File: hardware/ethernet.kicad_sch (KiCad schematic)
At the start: 98 parts, among them J5 USB_C_Receptacle, Q1 BSS138, Q2 BSS138, U11 TXS0202YZPR, U14 KSZ9031RNXCA, U4 CCGM1A1, X1 ECS-2520MV-250-xx

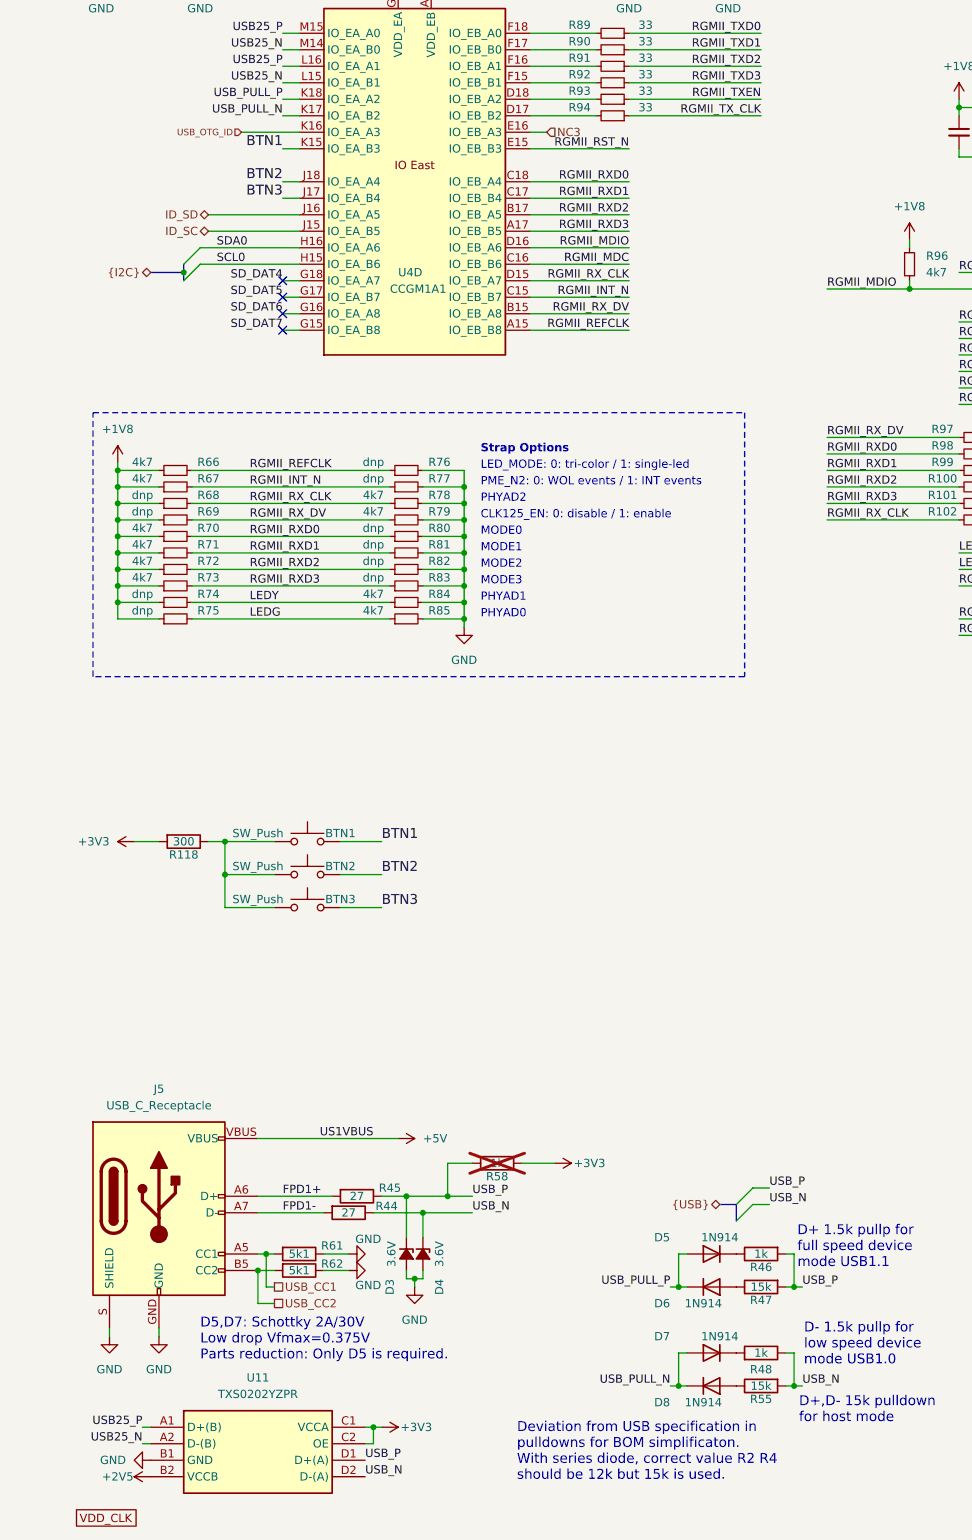
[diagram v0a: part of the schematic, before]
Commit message: Clearing all ERC, rounting diff
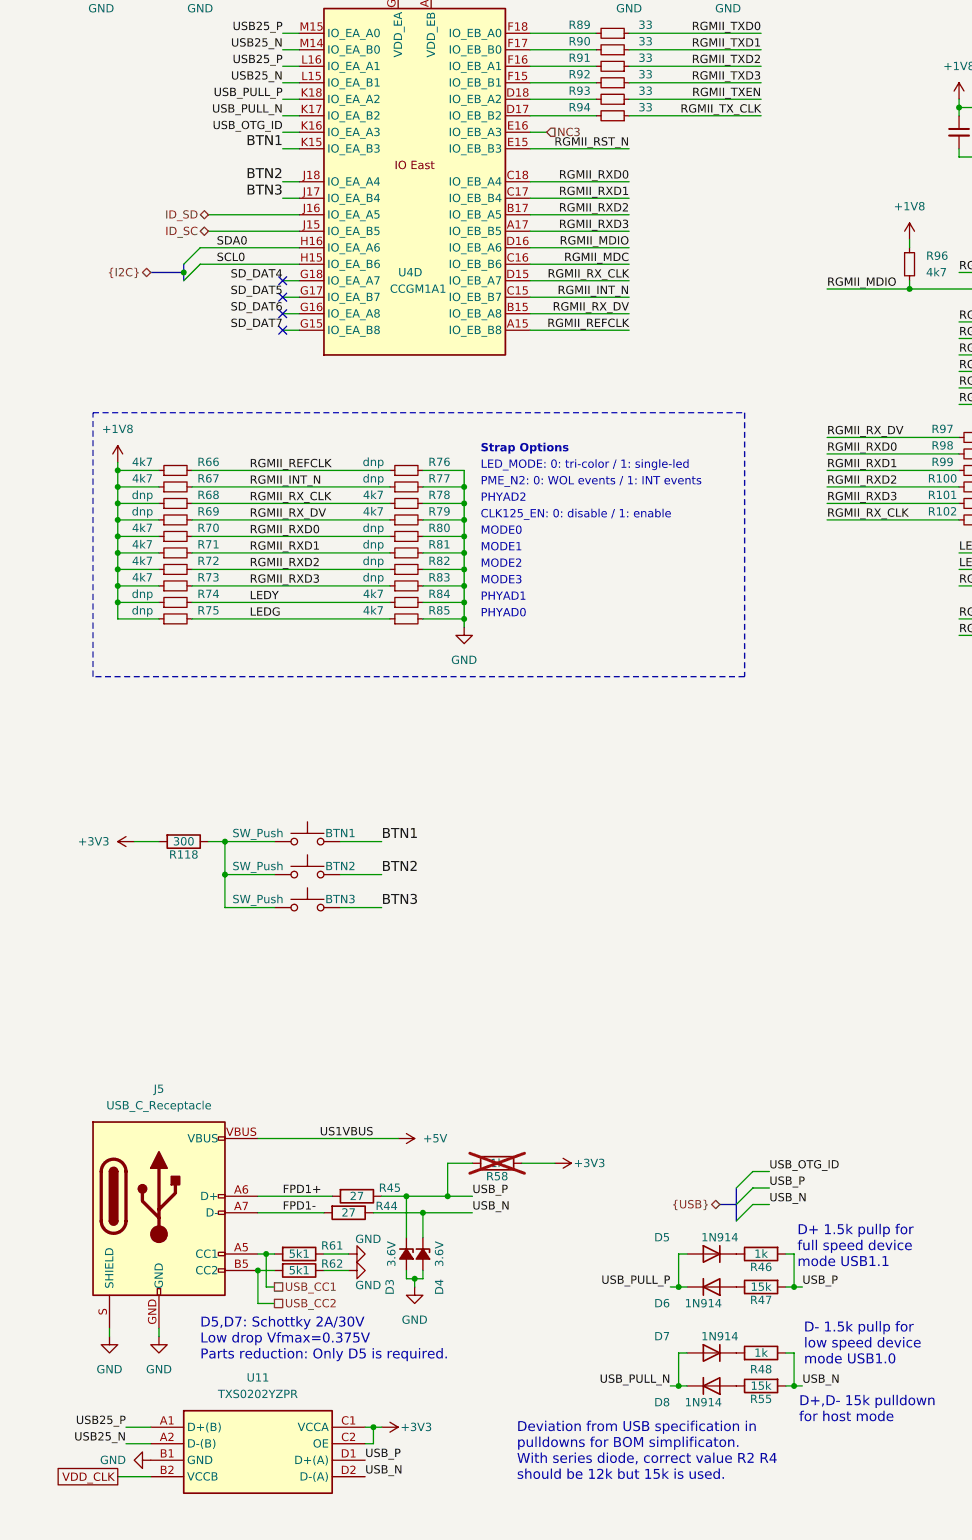
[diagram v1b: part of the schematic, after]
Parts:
- U11: footprint TXS0202:BGA8C50P2X4_89X189X50 -> TXS0202YZPR:BGA8C50P2X4_89X189X50
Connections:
- net +2V5 is gone; now on net VDD_CLK: U11.B2 (VCCB)
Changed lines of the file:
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@@
 	)
 	(bus_entry
+		(at 125.73 219.71)
+		(size -2.54 2.54)
+		(stroke
+			(width 0)
+			(type default)
+		)
+	)
+	(bus_entry
 		(at 248.92 109.22)
 		(size 2.54 2.54)
@@
 	(wire
 		(pts
-			(xy 31.75 261.62) (xy 33.02 261.62)
+			(xy 29.21 261.62) (xy 33.02 261.62)
 		)
 		(stroke
@@
 	(wire
 		(pts
+			(xy 125.73 219.71) (xy 128.27 219.71)
+		)
+		(stroke
+			(width 0)
+			(type default)
+		)
+	)
+	(wire
+		(pts
 			(xy 41.91 168.91) (xy 44.45 168.91)
 		)
@@
 		)
 	)
+	(bus
+		(pts
+			(xy 123.19 222.25) (xy 123.19 224.79)
+		)
+		(stroke
+			(width 0)
+			(type default)
+		)
+	)
 	(wire
 		(pts
@@
 	(wire
 		(pts
-			(xy 46.99 59.69) (xy 55.88 59.69)
+			(xy 53.34 59.69) (xy 55.88 59.69)
 		)
 		(stroke
@@
 	(wire
 		(pts
-			(xy 31.75 259.08) (xy 33.02 259.08)
+			(xy 29.21 259.08) (xy 33.02 259.08)
 		)
 		(stroke
@@
 	(wire
 		(pts
+			(xy 27.94 266.7) (xy 33.02 266.7)
+		)
+		(stroke
+			(width 0)
+			(type default)
+		)
+	)
+	(wire
+		(pts
 			(xy 106.68 54.61) (xy 127 54.61)
 		)
@@
 	)
 	(label "USB25_P"
-		(at 31.75 259.08 180)
+		(at 29.21 259.08 180)
 		(effects
 			(font
@@
 		)
 	)
+	(label "USB_OTG_ID"
+		(at 128.27 219.71 0)
+		(effects
+			(font
+				(size 1.25 1.25)
+			)
+			(justify left bottom)
+		)
+	)
 	(label "USB25_N"
 		(at 53.34 46.99 180)
@@
 	)
 	(label "USB25_N"
-		(at 31.75 261.62 180)
+		(at 29.21 261.62 180)
 		(effects
 			(font
@@
 		)
 	)
+	(label "USB_OTG_ID"
+		(at 53.34 59.69 180)
+		(effects
+			(font
+				(size 1.25 1.25)
+			)
+			(justify right bottom)
+		)
+	)
 	(label "ETH1_P"
 		(at 248.92 119.38 180)
@@
 	(global_label "VDD_CLK"
 		(shape passive)
-		(at 21.59 273.05 0)
+		(at 27.94 266.7 180)
 		(fields_autoplaced yes)
 		(effects
@@
 				(size 1.27 1.27)
 			)
-			(justify left)
+			(justify right)
 		)
 		(property "Intersheetrefs" "${INTERSHEET_REFS}"
-			(at 31.6282 273.05 0)
+			(at 17.9018 266.7 0)
 			(effects
 				(font
 					(size 1.27 1.27)
 				)
-				(justify left)
+				(justify right)
 				(hide yes)
 			)
@@
 		)
 	)
-	(hierarchical_label "USB_OTG_ID"
-		(shape input)
-		(at 46.99 59.69 180)
-		(effects
-			(font
-				(size 1 1)
-			)
-			(justify right)
-		)
-	)
 	(hierarchical_label "NC3"
 		(shape input)
@@
 	)
 	(symbol
-		(lib_name "+5V_1")
-		(lib_id "power:+5V")
-		(at 33.02 266.7 90)
-		(unit 1)
-		(exclude_from_sim no)
-		(in_bom yes)
-		(on_board yes)
-		(dnp no)
-		(property "Reference" "#PWR0170"
-			(at 36.83 266.7 0)
-			(effects
-				(font
-					(size 1.27 1.27)
-				)
-				(hide yes)
-			)
-		)
-		(property "Value" "+2V5"
-			(at 27.94 266.7 90)
-			(effects
-				(font
-					(size 1.27 1.27)
-				)
-			)
-		)
-		(property "Footprint" ""
-			(at 33.02 266.7 0)
-			(effects
-				(font
-					(size 1.27 1.27)
-				)
-				(hide yes)
-			)
-		)
-		(property "Datasheet" ""
-			(at 33.02 266.7 0)
-			(effects
-				(font
-					(size 1.27 1.27)
-				)
-				(hide yes)
-			)
-		)
-		(property "Description" "Power symbol creates a global label with name \"+5V\""
-			(at 33.02 266.7 0)
-			(effects
-				(font
-					(size 1.27 1.27)
-				)
-				(hide yes)
-			)
-		)
-		(pin "1"
-		)
-		(instances
-			(project "ulx5m-gs"
-				(path "/9e5cbfd6-8186-4817-919e-acd256336bc8/5c4580e2-a442-496c-941e-38ded55dcc84"
-					(reference "#PWR0170")
-					(unit 1)
-				)
-			)
-		)
-	)
-	(symbol
 		(lib_id "Device:R")
 		(at 38.1 168.91 270)
@@
 			)
 		)
-		(property "Footprint" "TXS0202:BGA8C50P2X4_89X189X50"
+		(property "Footprint" "TXS0202YZPR:BGA8C50P2X4_89X189X50"
 			(at 62.23 354 0)
 			(effects

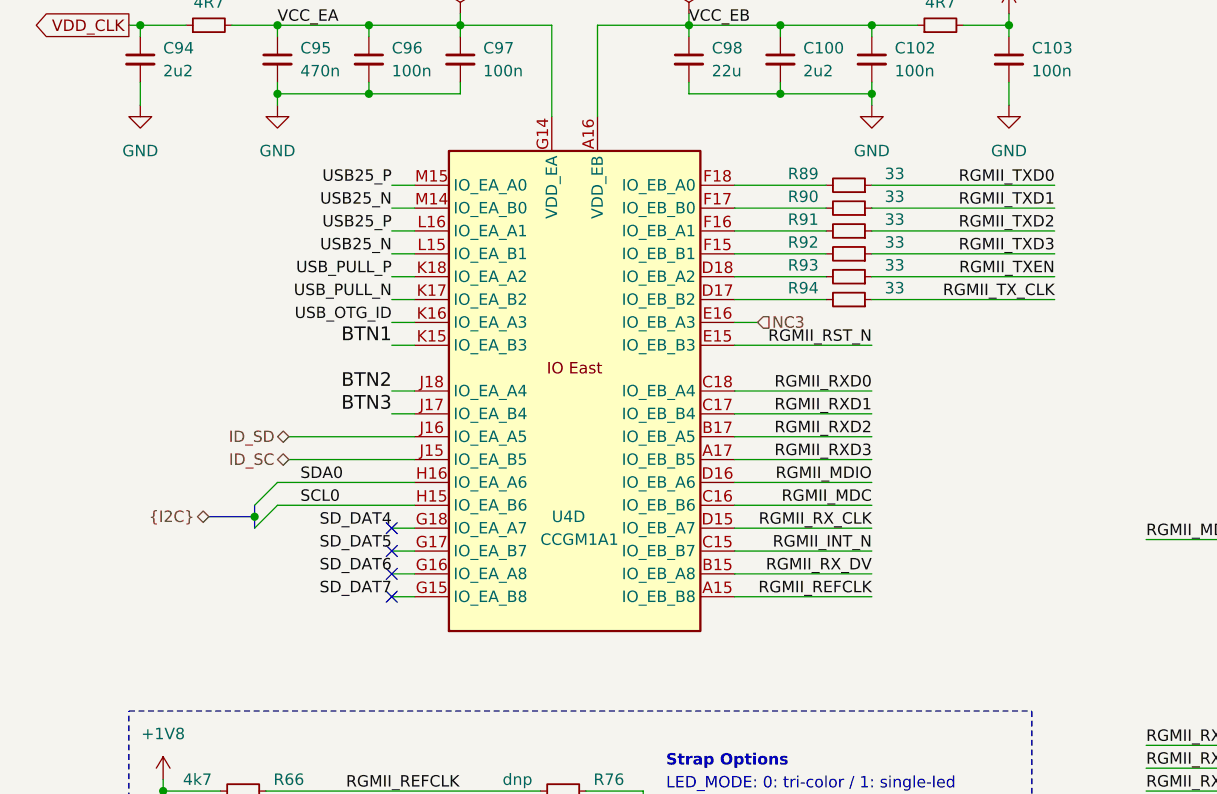
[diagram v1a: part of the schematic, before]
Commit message: Routing BTNs, LEDs, CLK
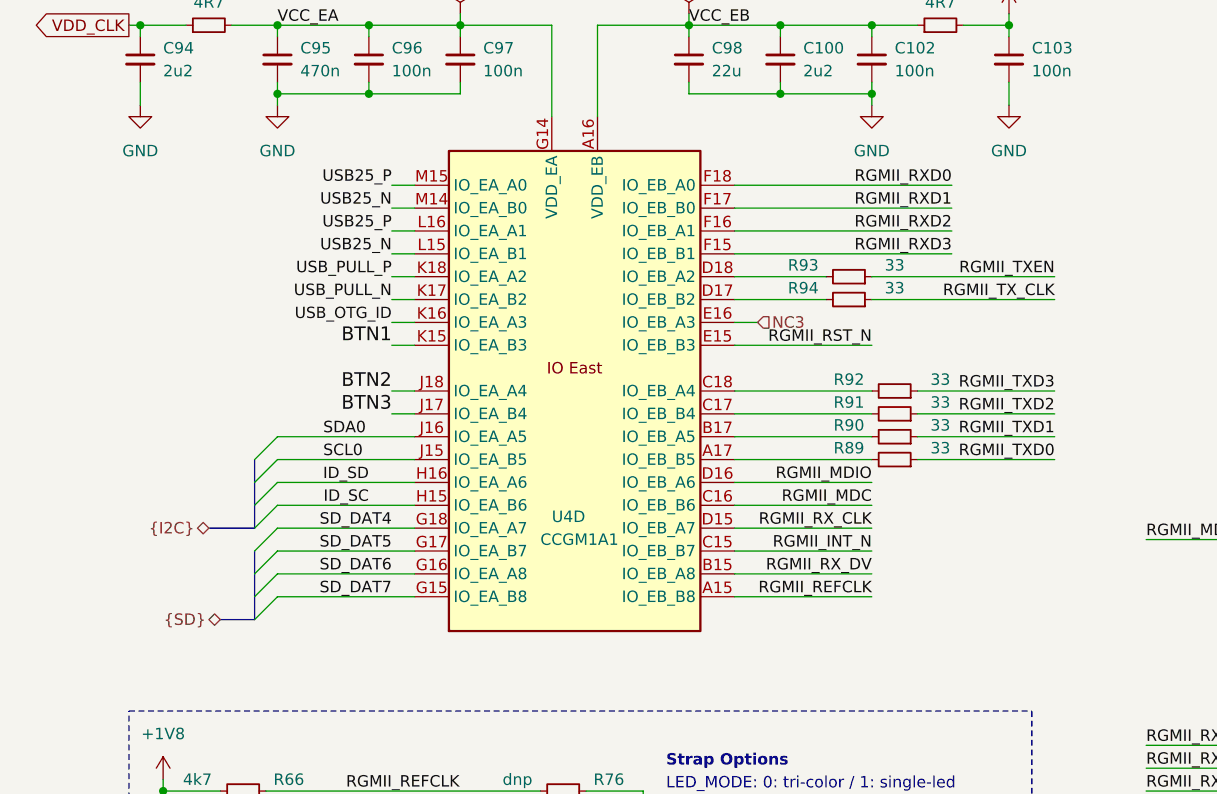
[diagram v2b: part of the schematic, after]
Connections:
- net ID_SC: now also U4.H15 (IO_EA_B6); no longer U4.J15 (IO_EA_B5)
- net ID_SD: now also U4.H16 (IO_EA_A6); no longer U4.J16 (IO_EA_A5)
- net RGMII_RXD0: now also U4.F18 (IO_EB_A0); no longer U4.C18 (IO_EB_A4)
- net RGMII_RXD1: now also U4.F17 (IO_EB_B0); no longer U4.C17 (IO_EB_B4)
- net RGMII_RXD2: now also U4.F16 (IO_EB_A1); no longer U4.B17 (IO_EB_A5)
- net RGMII_RXD3: now also U4.F15 (IO_EB_B1); no longer U4.A17 (IO_EB_B5)
- net SCL0: now also U4.J15 (IO_EA_B5); no longer U4.H15 (IO_EA_B6)
- net SDA0: now also U4.J16 (IO_EA_A5); no longer U4.H16 (IO_EA_A6)
- net at R92.2: now also U4.C18 (IO_EB_A4); no longer U4.F15 (IO_EB_B1)
- net at R91.2: now also U4.C17 (IO_EB_B4); no longer U4.F16 (IO_EB_A1)
- net at R90.2: now also U4.B17 (IO_EB_A5); no longer U4.F17 (IO_EB_B0)
- net at R89.2: now also U4.A17 (IO_EB_B5); no longer U4.F18 (IO_EB_A0)
- no-connect marks 14 -> 10
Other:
- moved on the sheet: R89, R90, R91, R92

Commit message: Cleanup
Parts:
- removed C67, C68, C69, C70, C71, C72, C73, C74: 10n, Capacitor_SMD:C_0402_1005Metric, symbol Device:C_Small
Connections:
- no-connect marks 10 -> 2
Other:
- moved on the sheet: BTN1, BTN2, BTN3, D3, D4, D5, D6, D7, D8, J5, R118, R44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

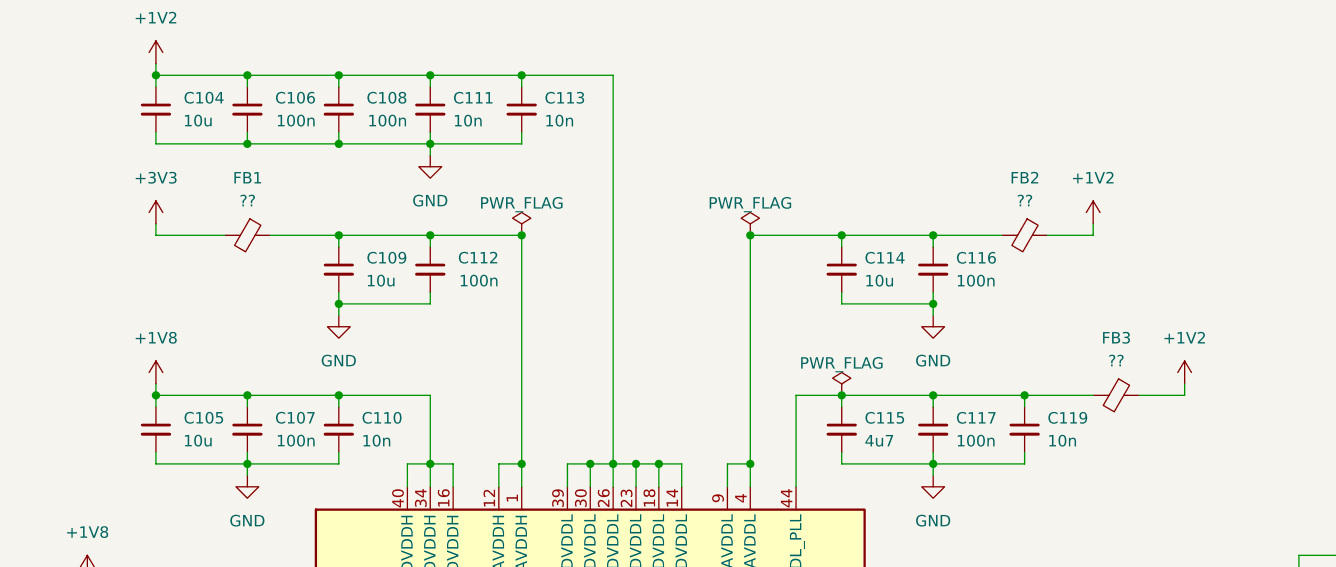
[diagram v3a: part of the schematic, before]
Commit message: Adding L1, L2, L3, L4 FB1,FB2, FB3 parts, changing name under FPGA
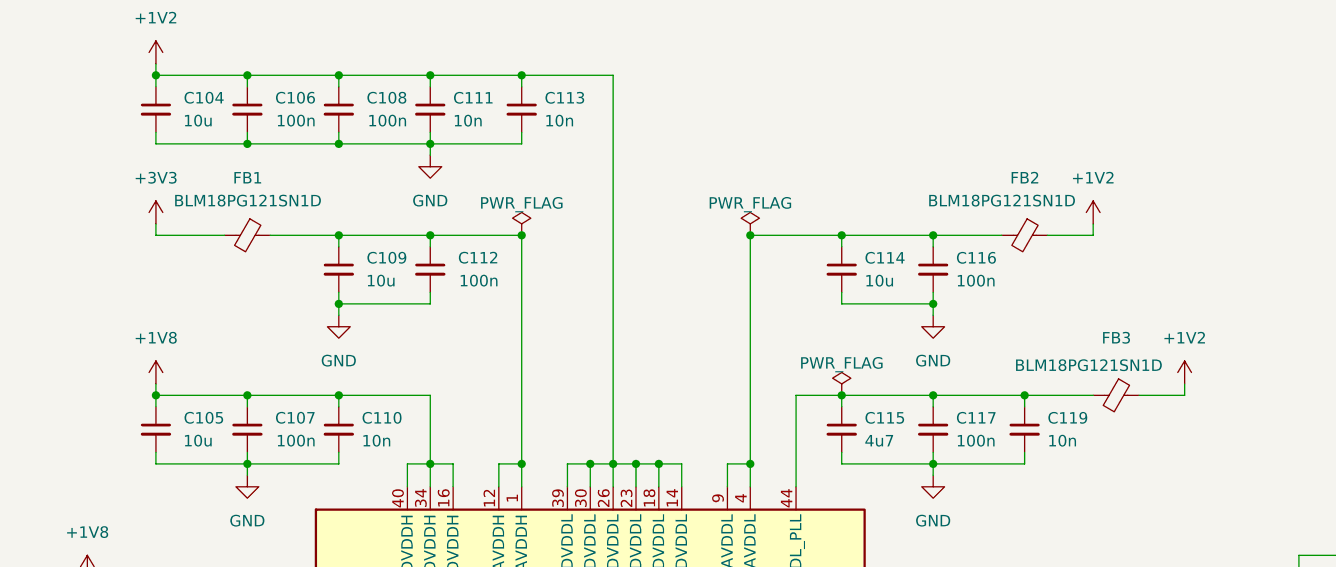
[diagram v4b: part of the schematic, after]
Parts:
- FB1, FB2, FB3: value ?? -> BLM18PG121SN1D; Mouser (none) -> https://hr.mouser.com/ProductDetail/Murata-Electronics/BLM1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
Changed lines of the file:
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@@
 		(on_board yes)
 		(dnp no)
-		(fields_autoplaced yes)
 		(property "Reference" "FB3"
 			(at 264.1981 49.53 90)
@@
 			)
 		)
-		(property "Value" "??"
-			(at 264.1981 52.07 90)
+		(property "Value" "BLM18PG121SN1D"
+			(at 261.112 52.578 90)
 			(effects
 				(font
@@
 			)
 		)
+		(property "Mouser" "https://hr.mouser.com/ProductDetail/Murata-Electronics/BLM18PG121SN1D?qs=tY8e8KZalarVxhnmnUYZ1A%3D%3D"
+			(at 264.16 55.88 0)
+			(effects
+				(font
+					(size 1.27 1.27)
+				)
+				(hide yes)
+			)
+		)
 		(pin "2"
 		)
@@
 			)
 		)
-		(property "Value" "??"
+		(property "Value" "BLM18PG121SN1D"
 			(at 167.6781 34.29 90)
 			(effects
@@
 			)
 		)
+		(property "Mouser" "https://hr.mouser.com/ProductDetail/Murata-Electronics/BLM18PG121SN1D?qs=tY8e8KZalarVxhnmnUYZ1A%3D%3D"
+			(at 167.64 38.1 0)
+			(effects
+				(font
+					(size 1.27 1.27)
+				)
+				(hide yes)
+			)
+		)
 		(pin "2"
 		)
@@
 		(on_board yes)
 		(dnp no)
-		(fields_autoplaced yes)
 		(property "Reference" "FB2"
 			(at 254.0381 31.75 90)
@@
 			)
 		)
-		(property "Value" "??"
-			(at 254.0381 34.29 90)
+		(property "Value" "BLM18PG121SN1D"
+			(at 251.46 34.29 90)
 			(effects
 				(font
@@
 			)
 		)
+		(property "Mouser" "https://hr.mouser.com/ProductDetail/Murata-Electronics/BLM18PG121SN1D?qs=tY8e8KZalarVxhnmnUYZ1A%3D%3D"
+			(at 254 38.1 0)
+			(effects
+				(font
+					(size 1.27 1.27)
+				)
+				(hide yes)
+			)
+		)
